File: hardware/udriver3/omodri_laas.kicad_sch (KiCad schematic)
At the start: 19 parts, among them J1 conn_01x04_MountingPins

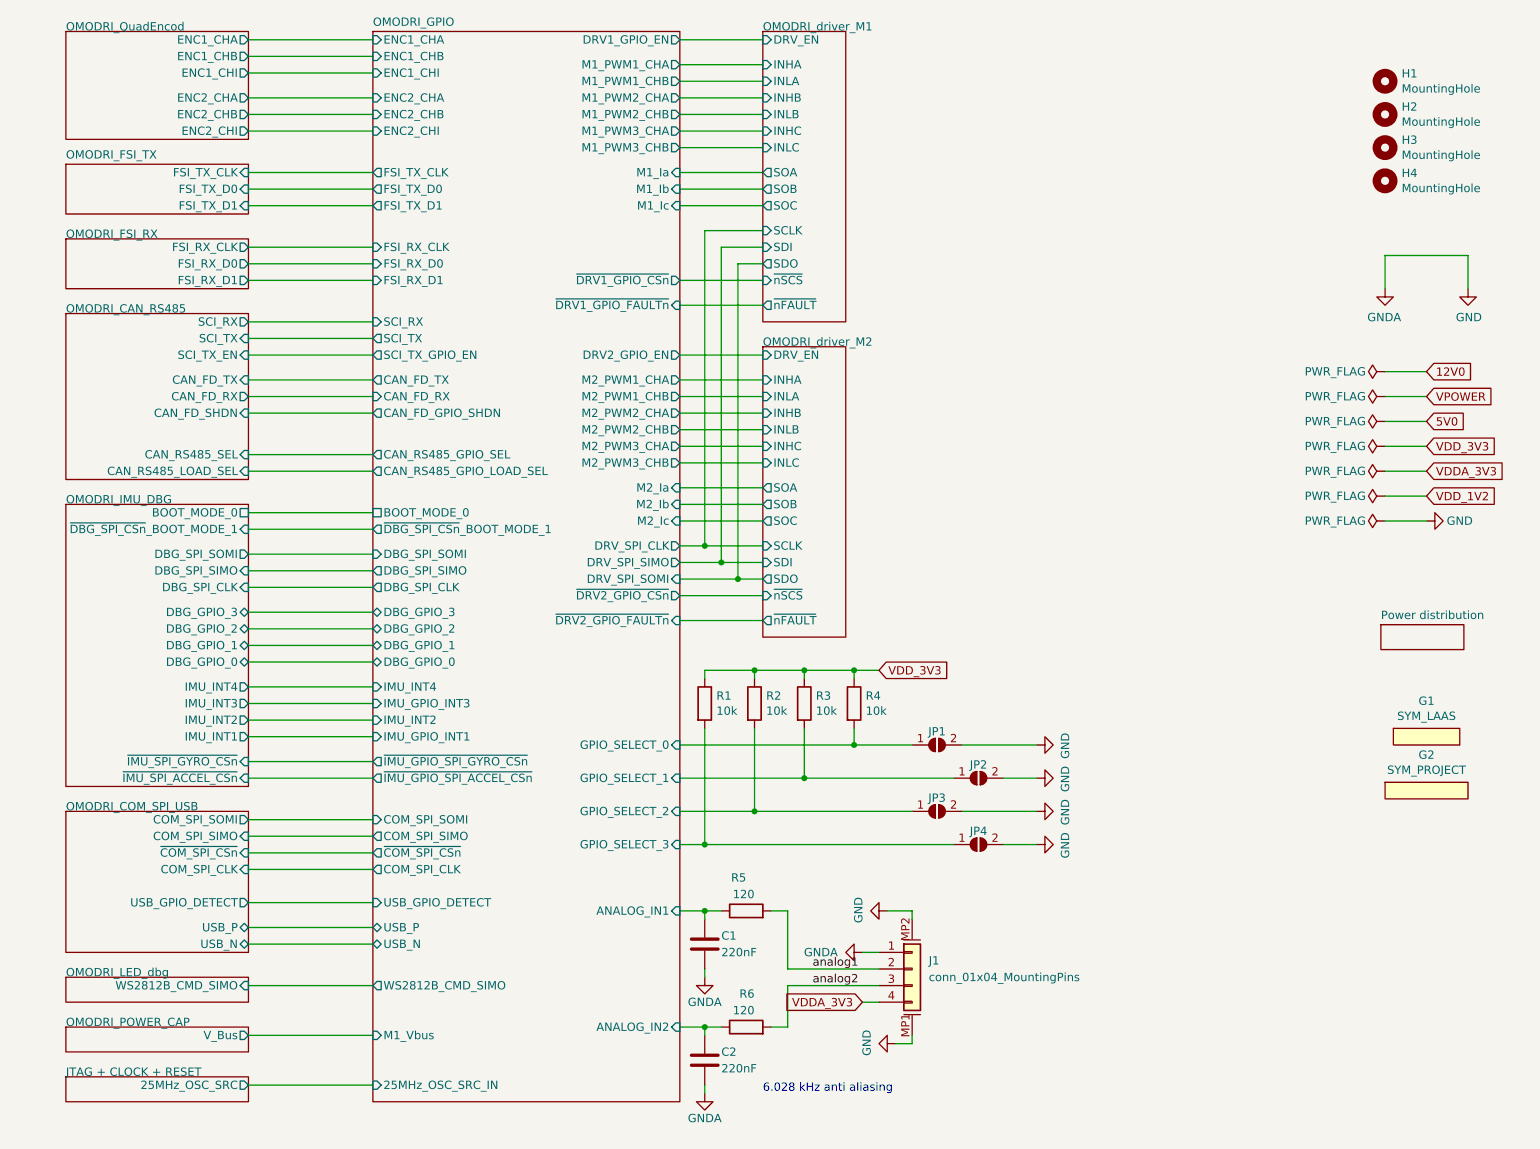
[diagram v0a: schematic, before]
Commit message: update 3D models. Modify the SPI CS debug pin previously shared with boot function. Regen gerber files.
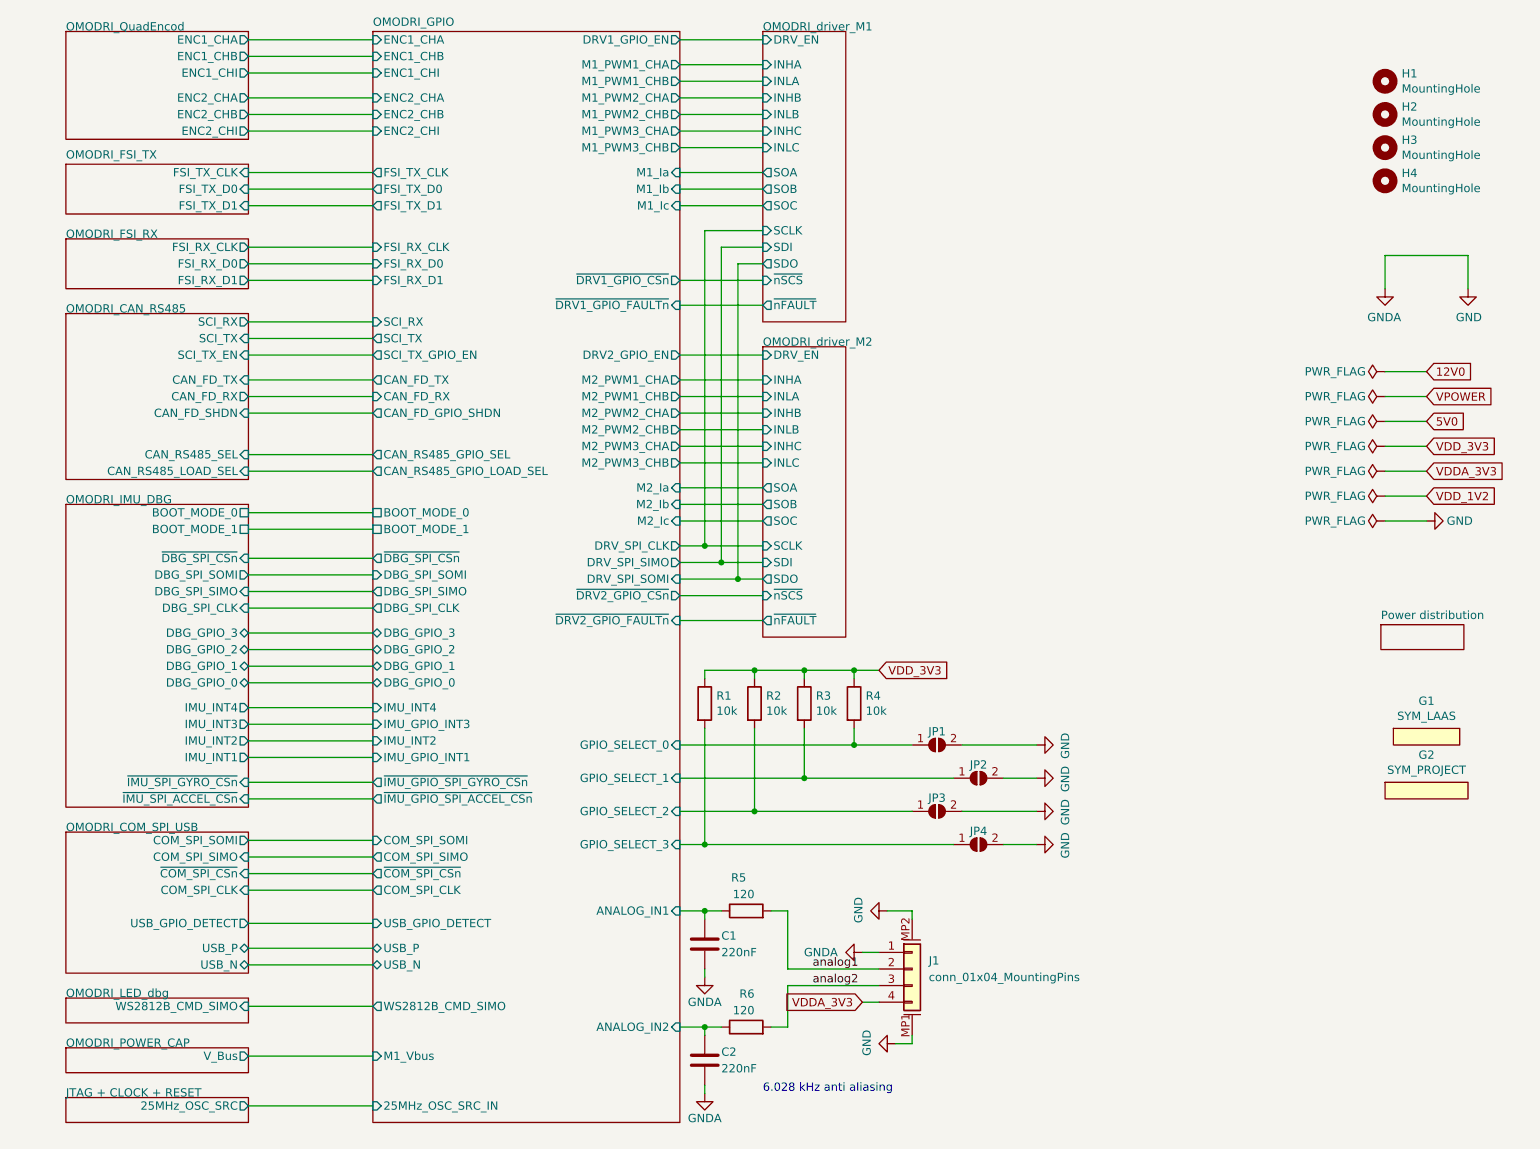
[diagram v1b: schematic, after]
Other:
- sheet OMODRI_GPIO ports: added BOOT_MODE_1, ~{DBG_SPI_CSn}; removed ~{DBG_SPI_CSn}_BOOT_MODE_1
- sheet OMODRI_IMU_DBG ports: added BOOT_MODE_1, ~{DBG_SPI_CSn}; removed ~{DBG_SPI_CSn}_BOOT_MODE_1

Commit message: Update of the load connect/disconnect on the CAN/RS485 bus. Remove the electronic switch replaced by a 1.27mm jumper.
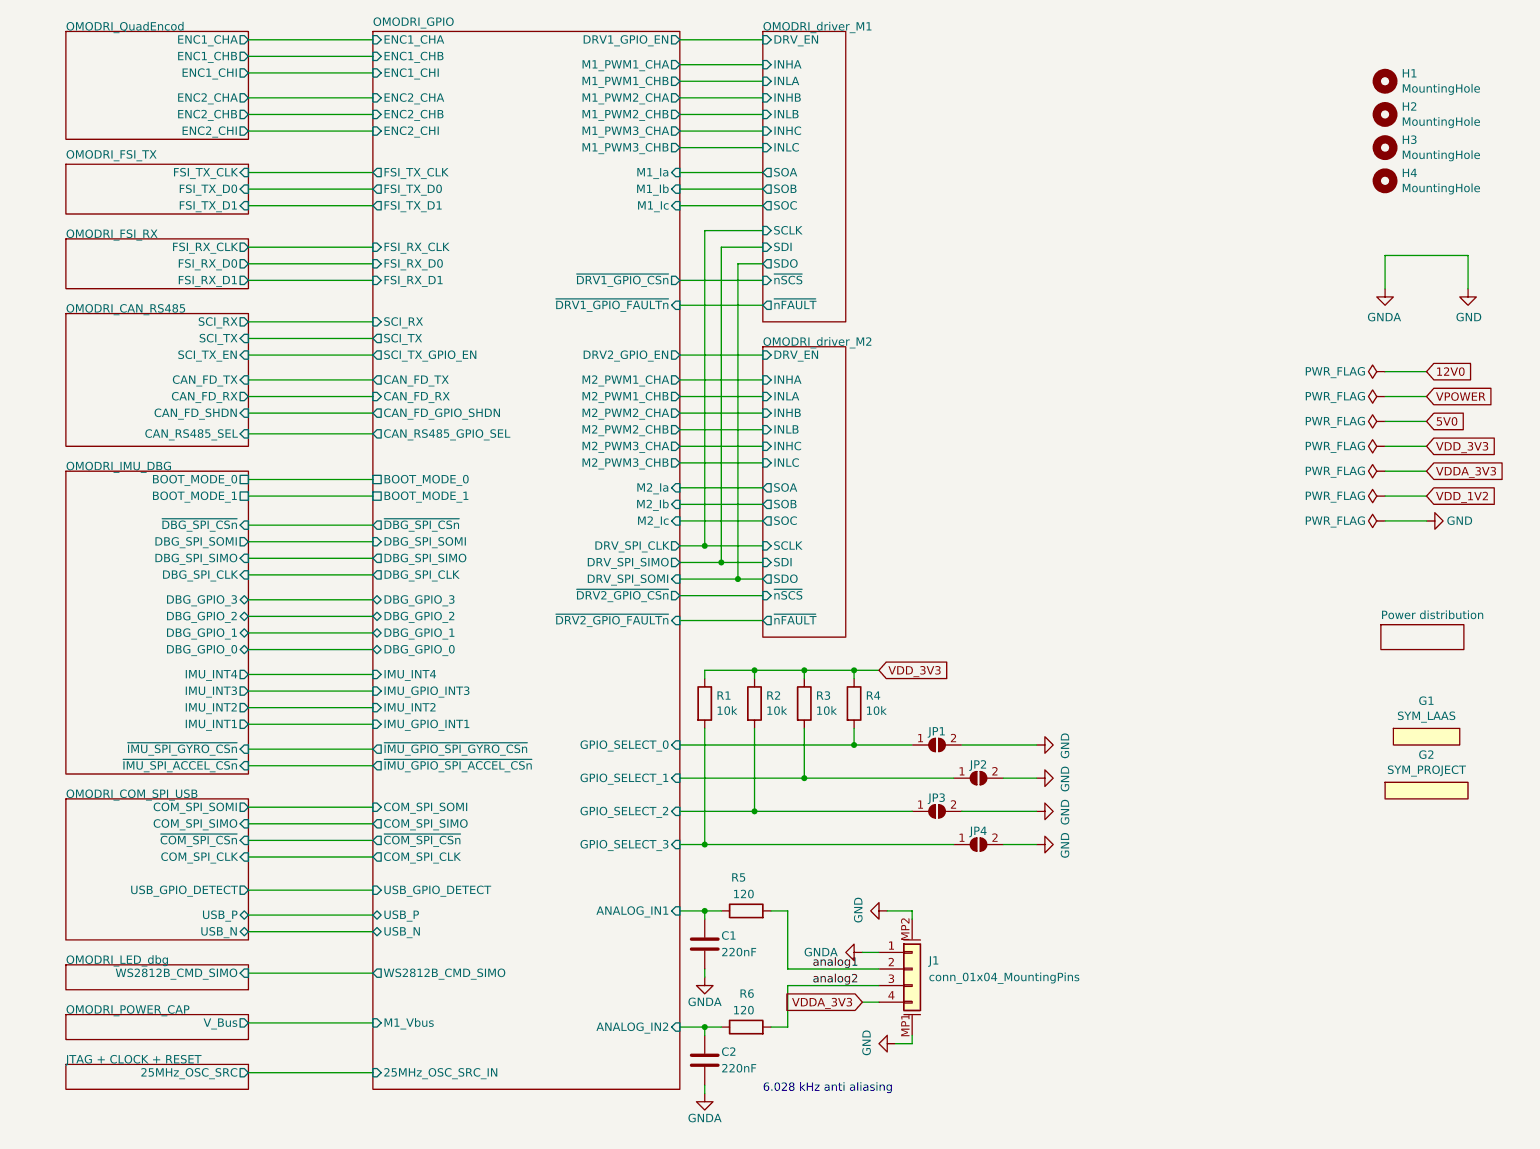
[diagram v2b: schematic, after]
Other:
- sheet OMODRI_CAN_RS485 ports: added none; removed CAN_RS485_LOAD_SEL
- sheet OMODRI_GPIO ports: added none; removed CAN_RS485_GPIO_LOAD_SEL

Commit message: Add JLCPCB components ref where it was matching.
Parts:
- J1: LCSC (none) -> C597873
- R1, R2, R3, R4: LCSC (none) -> C9900024792
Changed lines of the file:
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@@
+      (effects (font (size 1.27 1.27)) hide)
+    )
+    (property "LCSC" "" (at 228.6 26.67 0)
       (effects (font (size 1.27 1.27)) hide)
     )
@@
       (effects (font (size 1.27 1.27)) hide)
     )
+    (property "LCSC" "" (at 228.6 31.75 0)
+      (effects (font (size 1.27 1.27)) hide)
+    )
     (instances
       (project "omodri_laas"
@@
       (effects (font (size 1.27 1.27)) hide)
     )
+    (property "LCSC" "" (at 228.6 36.83 0)
+      (effects (font (size 1.27 1.27)) hide)
+    )
     (instances
       (project "omodri_laas"
@@
       (effects (font (size 1.27 1.27)) hide)
     )
+    (property "LCSC" "" (at 228.6 41.91 0)
+      (effects (font (size 1.27 1.27)) hide)
+    )
     (instances
       (project "omodri_laas"
@@
       (effects (font (size 1.27 1.27)) hide)
     )
+    (property "LCSC" "" (at 130.81 153.67 0)
+      (effects (font (size 1.27 1.27)) hide)
+    )
     (pin "1")
     (pin "2")
@@
       (effects (font (size 1.27 1.27)) hide)
     )
+    (property "LCSC" "" (at 124.46 158.75 0)
+      (effects (font (size 1.27 1.27)) hide)
+    )
     (pin "1")
     (pin "2")
@@
       (effects (font (size 1.27 1.27)) hide)
     )
+    (property "LCSC" "" (at 130.81 171.45 0)
+      (effects (font (size 1.27 1.27)) hide)
+    )
     (pin "1")
     (pin "2")
@@
     )
     (property "Rated Voltage" "16V" (at 124.46 176.53 0)
+      (effects (font (size 1.27 1.27)) hide)
+    )
+    (property "LCSC" "" (at 124.46 176.53 0)
       (effects (font (size 1.27 1.27)) hide)
     )
@@
       (effects (font (size 1.27 1.27)) hide)
     )
+    (property "LCSC" "" (at 234.95 127 0)
+      (effects (font (size 1.27 1.27)) hide)
+    )
     (instances
       (project "omodri_laas"
@@
       (effects (font (size 1.27 1.27)) hide)
     )
+    (property "LCSC" "" (at 234.95 135.255 0)
+      (effects (font (size 1.27 1.27)) hide)
+    )
     (instances
       (project "omodri_laas"
@@
       (effects (font (size 1.27 1.27)) hide)
     )
+    (property "LCSC" "" (at 160.02 138.43 0)
+      (effects (font (size 1.27 1.27)) hide)
+    )
     (pin "1")
     (pin "2")
@@
       (effects (font (size 1.27 1.27)) hide)
     )
+    (property "LCSC" "" (at 166.37 133.35 0)
+      (effects (font (size 1.27 1.27)) hide)
+    )
     (pin "1")
     (pin "2")
@@
       (effects (font (size 1.27 1.27)) hide)
     )
+    (property "LCSC" "C9900024792" (at 147.32 121.92 0)
+      (effects (font (size 1.27 1.27)) hide)
+    )
     (pin "1")
     (pin "2")
@@
     )
     (property "RS" "176-3597" (at 139.7 121.92 0)
+      (effects (font (size 1.27 1.27)) hide)
+    )
+    (property "LCSC" "C9900024792" (at 139.7 121.92 0)
       (effects (font (size 1.27 1.27)) hide)
     )
@@
       (effects (font (size 1.27 1.27)) hide)
     )
+    (property "LCSC" "" (at 166.37 143.51 0)
+      (effects (font (size 1.27 1.27)) hide)
+    )
     (pin "1")
     (pin "2")
@@
     )
     (property "RS" "188-6267" (at 156.21 163.83 0)
+      (effects (font (size 1.27 1.27)) hide)
+    )
+    (property "LCSC" "C597873" (at 156.21 163.83 0)
       (effects (font (size 1.27 1.27)) hide)
     )
@@
       (effects (font (size 1.27 1.27)) hide)
     )
+    (property "LCSC" "C9900024792" (at 132.08 121.92 0)
+      (effects (font (size 1.27 1.27)) hide)
+    )
     (pin "1")
     (pin "2")
@@
       (effects (font (size 1.27 1.27)) hide)
     )
+    (property "LCSC" "" (at 160.02 128.27 0)
+      (effects (font (size 1.27 1.27)) hide)
+    )
     (pin "1")
     (pin "2")
@@
       (effects (font (size 1.27 1.27)) hide)
     )
+    (property "LCSC" "C9900024792" (at 124.46 121.92 0)
+      (effects (font (size 1.27 1.27)) hide)
+    )

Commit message: Update PCB layout to match JLCPCB requirements (via diameter). Set Netclass constraints defined in uOmodri_v2.
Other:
- moved on the sheet: C1, C2, J1, R5, R6

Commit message: Add snubbers on motors phases & resistors on high side gates. Update BOM list.
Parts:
- C1, C2: DigiKey 490-GRM033R61C224KE14JTR-ND -> 490-17040-1-ND; Farnell 3785715 -> 3582770; LCSC (none) -> C161474; Mouser 81-GRM033R61C224KE4J -> 81-GRM033R61C224KE4D; Part No GRM033R61C224KE14J -> GRM033R61C224KE14D
- JP1, JP2, JP3, JP4: now left out of the parts list
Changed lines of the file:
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@@
 			)
 		)
-		(property "DigiKey" "490-GRM033R61C224KE14JTR-ND"
+		(property "DigiKey" "490-17040-1-ND"
 			(at 127 160.02 0)
 			(effects
@@
 			)
 		)
-		(property "Farnell" "3785715"
+		(property "Farnell" "3582770"
 			(at 127 160.02 0)
 			(effects
@@
 			)
 		)
-		(property "Mouser" "81-GRM033R61C224KE4J"
+		(property "Mouser" "81-GRM033R61C224KE4D"
 			(at 127 160.02 0)
 			(effects
@@
 			)
 		)
-		(property "Part No" "GRM033R61C224KE14J"
+		(property "Part No" "GRM033R61C224KE14D"
 			(at 127 160.02 0)
 			(effects
@@
 			)
 		)
-		(property "LCSC" ""
+		(property "LCSC" "C161474"
 			(at 127 160.02 0)
 			(effects
@@
 			)
 		)
-		(property "DigiKey" "490-GRM033R61C224KE14JTR-ND"
+		(property "DigiKey" "490-17040-1-ND"
 			(at 127 177.8 0)
 			(effects
@@
 			)
 		)
-		(property "Farnell" "3785715"
+		(property "Farnell" "3582770"
 			(at 127 177.8 0)
 			(effects
@@
 			)
 		)
-		(property "Mouser" "81-GRM033R61C224KE4J"
+		(property "Mouser" "81-GRM033R61C224KE4D"
 			(at 127 177.8 0)
 			(effects
@@
 			)
 		)
-		(property "Part No" "GRM033R61C224KE14J"
+		(property "Part No" "GRM033R61C224KE14D"
 			(at 127 177.8 0)
 			(effects
@@
 			)
 		)
-		(property "LCSC" ""
+		(property "LCSC" "C161474"
 			(at 127 177.8 0)
 			(effects
@@
 		(unit 1)
 		(exclude_from_sim no)
-		(in_bom yes)
+		(in_bom no)
 		(on_board yes)
 		(dnp no)
@@
 		(unit 1)
 		(exclude_from_sim no)
-		(in_bom yes)
+		(in_bom no)
 		(on_board yes)
 		(dnp no)
@@
 		(unit 1)
 		(exclude_from_sim no)
-		(in_bom yes)
+		(in_bom no)
 		(on_board yes)
 		(dnp no)
@@
 		(unit 1)
 		(exclude_from_sim no)
-		(in_bom yes)
-		(on_board yes)
-		(dnp no)
+		(in_bom no)
+		(on_board yes)
+		(dnp no)

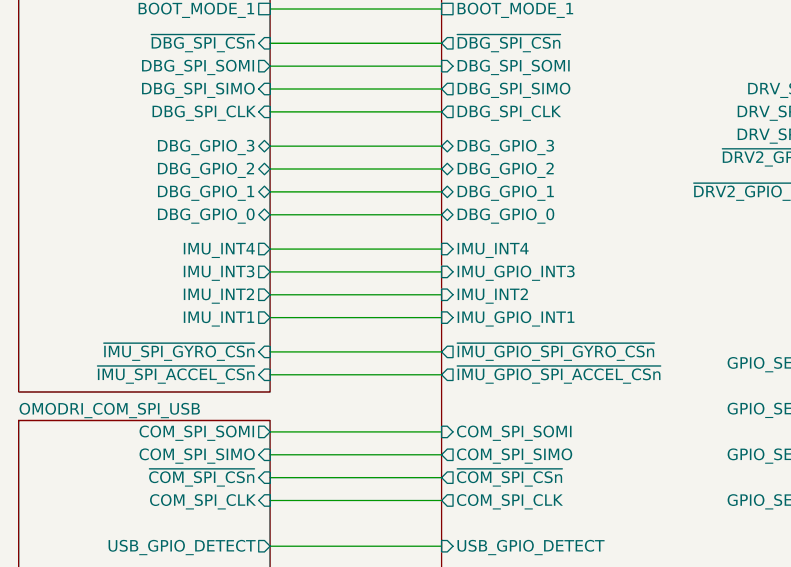
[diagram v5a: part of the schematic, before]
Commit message: Update of uOmodri_V3 replacing TCAN3413 by TCAN330G and adding sync on IMU.
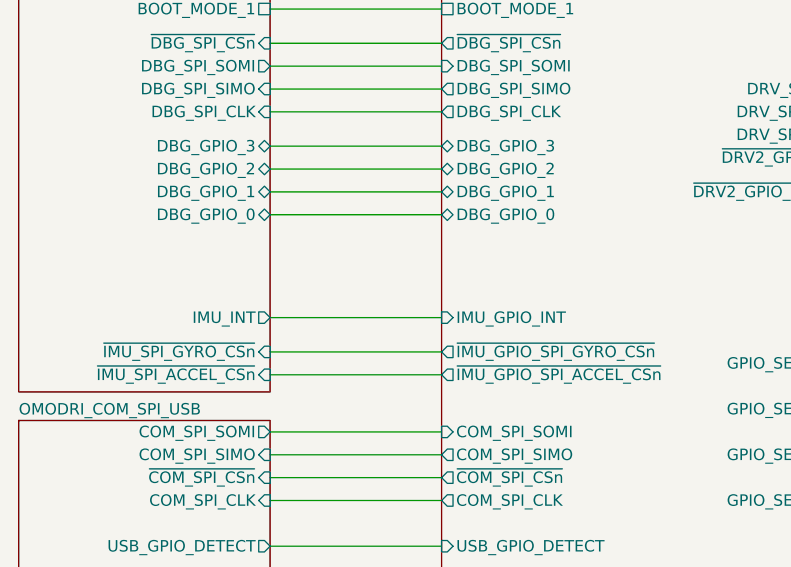
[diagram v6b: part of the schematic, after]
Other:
- sheet OMODRI_GPIO ports: added IMU_GPIO_INT; removed IMU_GPIO_INT1, IMU_GPIO_INT3, IMU_INT2, IMU_INT4
- sheet OMODRI_IMU_DBG ports: added IMU_INT; removed IMU_INT1, IMU_INT2, IMU_INT3, IMU_INT4
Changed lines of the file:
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@@
 	(wire
 		(pts
+			(xy 54.61 123.19) (xy 73.66 123.19)
+		)
+		(stroke
+			(width 0)
+			(type default)
+		)
+	)
+	(wire
+		(pts
 			(xy 147.32 125.73) (xy 147.32 128.27)
 		)
@@
 	(wire
 		(pts
-			(xy 54.61 120.65) (xy 73.66 120.65)
-		)
-		(stroke
-			(width 0)
-			(type default)
-		)
-	)
-	(wire
-		(pts
 			(xy 54.61 127) (xy 73.66 127)
 		)
@@
 	(wire
 		(pts
-			(xy 54.61 123.19) (xy 73.66 123.19)
-		)
-		(stroke
-			(width 0)
-			(type default)
-		)
-	)
-	(wire
-		(pts
 			(xy 241.3 53.34) (xy 241.3 58.42)
 		)
@@
 	(wire
 		(pts
-			(xy 54.61 115.57) (xy 73.66 115.57)
-		)
-		(stroke
-			(width 0)
-			(type default)
-		)
-	)
-	(wire
-		(pts
 			(xy 120.65 143.51) (xy 124.46 143.51)
 		)
@@
 	(wire
 		(pts
-			(xy 54.61 118.11) (xy 73.66 118.11)
-		)
-		(stroke
-			(width 0)
-			(type default)
-		)
-	)
-	(wire
-		(pts
 			(xy 170.18 133.35) (xy 173.99 133.35)
 		)
@@
 			)
 		)
-		(pin "IMU_INT2" input
-			(at 73.66 120.65 180)
-			(effects
-				(font
-					(size 1.27 1.27)
-				)
-				(justify left)
-			)
-		)
-		(pin "IMU_INT4" input
-			(at 73.66 115.57 180)
-			(effects
-				(font
-					(size 1.27 1.27)
-				)
-				(justify left)
-			)
-		)
 		(pin "WS2812B_CMD_SIMO" output
 			(at 73.66 160.02 180)
@@
 			)
 		)
-		(pin "IMU_GPIO_INT3" input
-			(at 73.66 118.11 180)
-			(effects
-				(font
-					(size 1.27 1.27)
-				)
-				(justify left)
-			)
-		)
 		(pin "~{IMU_GPIO_SPI_ACCEL_CSn}" output
 			(at 73.66 129.54 180)
@@
 			)
 		)
-		(pin "IMU_GPIO_INT1" input
+		(pin "IMU_GPIO_INT" input
 			(at 73.66 123.19 180)
 			(effects
@@
 			)
 		)
-		(pin "IMU_INT2" output
-			(at 54.61 120.65 0)
-			(effects
-				(font
-					(size 1.27 1.27)
-				)
-				(justify right)
-			)
-		)
-		(pin "IMU_INT4" output
-			(at 54.61 115.57 0)
-			(effects
-				(font
-					(size 1.27 1.27)
-				)
-				(justify right)
-			)
-		)
 		(pin "~{IMU_SPI_GYRO_CSn}" input
 			(at 54.61 127 0)
@@
 			)
 		)
-		(pin "IMU_INT3" output
-			(at 54.61 118.11 0)
-			(effects
-				(font
-					(size 1.27 1.27)
-				)
-				(justify right)
-			)
-		)
-		(pin "IMU_INT1" output
-			(at 54.61 123.19 0)
-			(effects
-				(font
-					(size 1.27 1.27)
-				)
-				(justify right)
-			)
-		)
 		(pin "DBG_GPIO_1" bidirectional
 			(at 54.61 109.22 0)
@@
 			(effects
 				(font
+					(size 1.27 1.27)
+				)
+				(justify right)
+			)
+		)
+		(pin "IMU_INT" output
+			(at 54.61 123.19 0)
+			(effects
+				(font

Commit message: Update of uOmodri V3. Correct pinning of CAN/RS485 connector.
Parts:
- J1: footprint udriver3:Hirose_DF13_04P-1.25H_1x05_P1.25mm_Right_angle -> udriver3:Hirose_DF13_04P-1.25H_1x04_P1.25mm_Right_angle
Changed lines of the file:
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@@
 	(title_block
 		(title "Open MOtor DRiver Initiative (OMODRI)")
-		(date "2024-02-29")
-		(rev "3.0")
+		(date "2024-05-03")
+		(rev "3.1")
 		(company "LAAS/CNRS")
 	)
@@
 			)
 		)
-		(property "Footprint" "udriver3:Hirose_DF13_04P-1.25H_1x05_P1.25mm_Right_angle"
+		(property "Footprint" "udriver3:Hirose_DF13_04P-1.25H_1x04_P1.25mm_Right_angle"
 			(at 158.75 166.37 0)
 			(effects
